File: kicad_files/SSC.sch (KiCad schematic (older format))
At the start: 9 parts, among them J1 Conn_01x09, J2 Conn_02x13_Top_Bottom, U1 74LS153, U2 74LS153

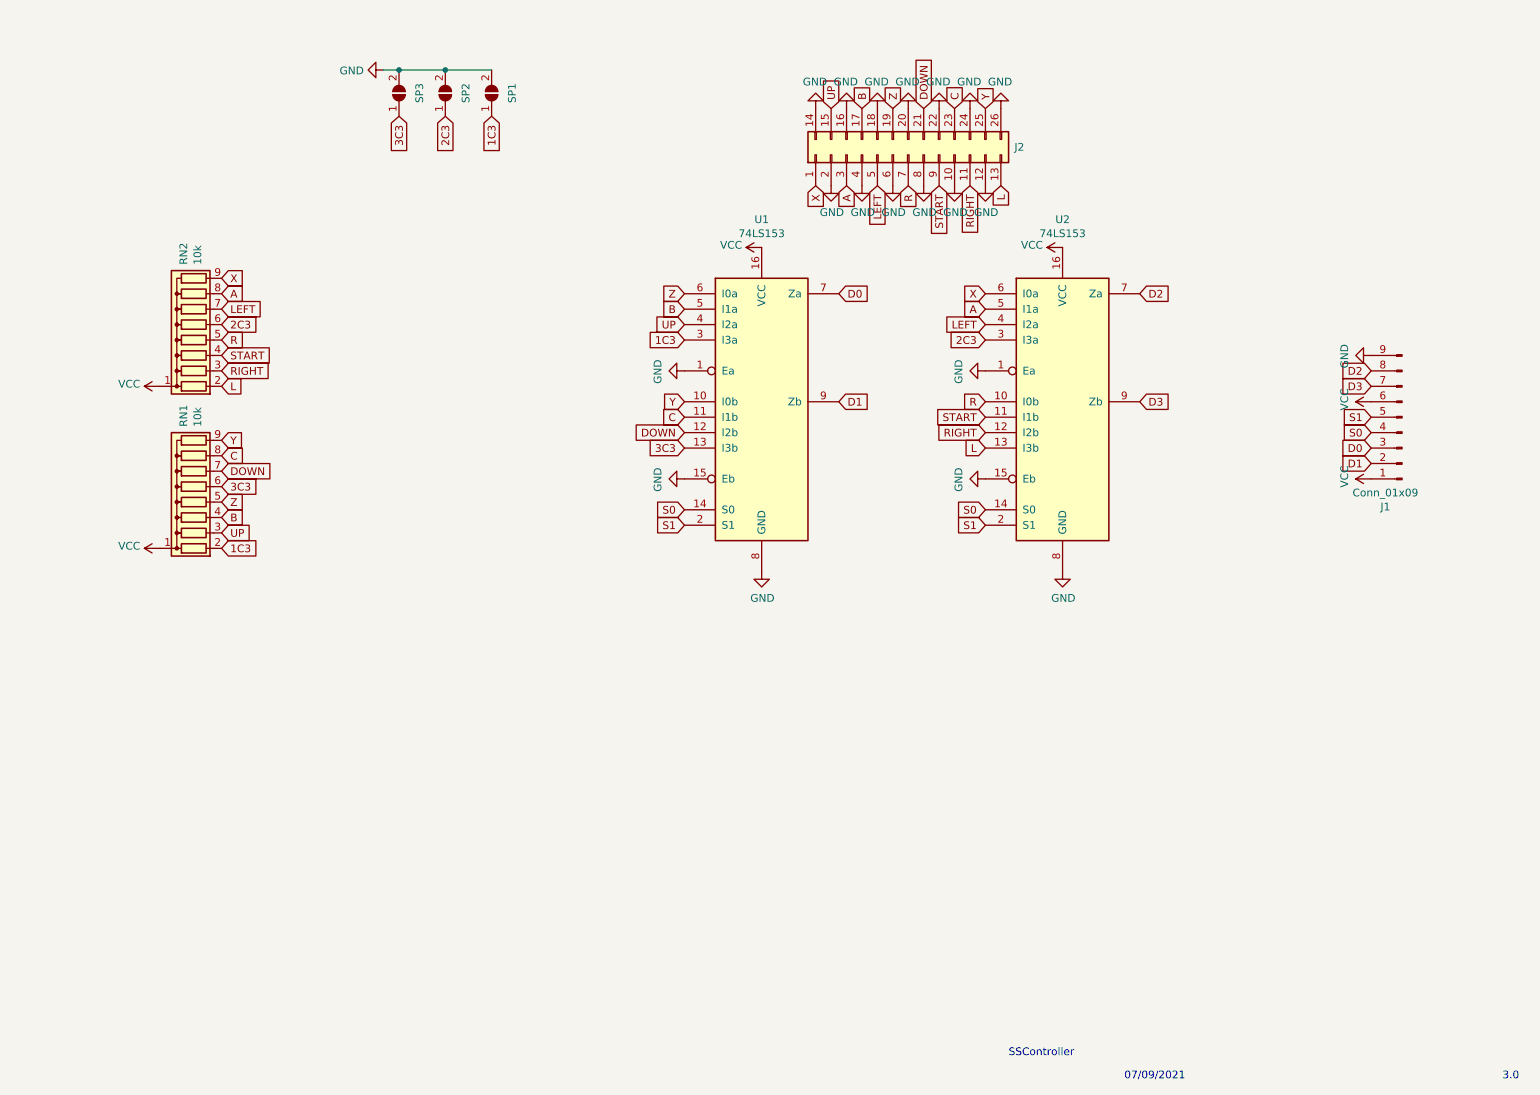
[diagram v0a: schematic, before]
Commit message: Add files via upload
Changed schematics a little and added holes to PCB.
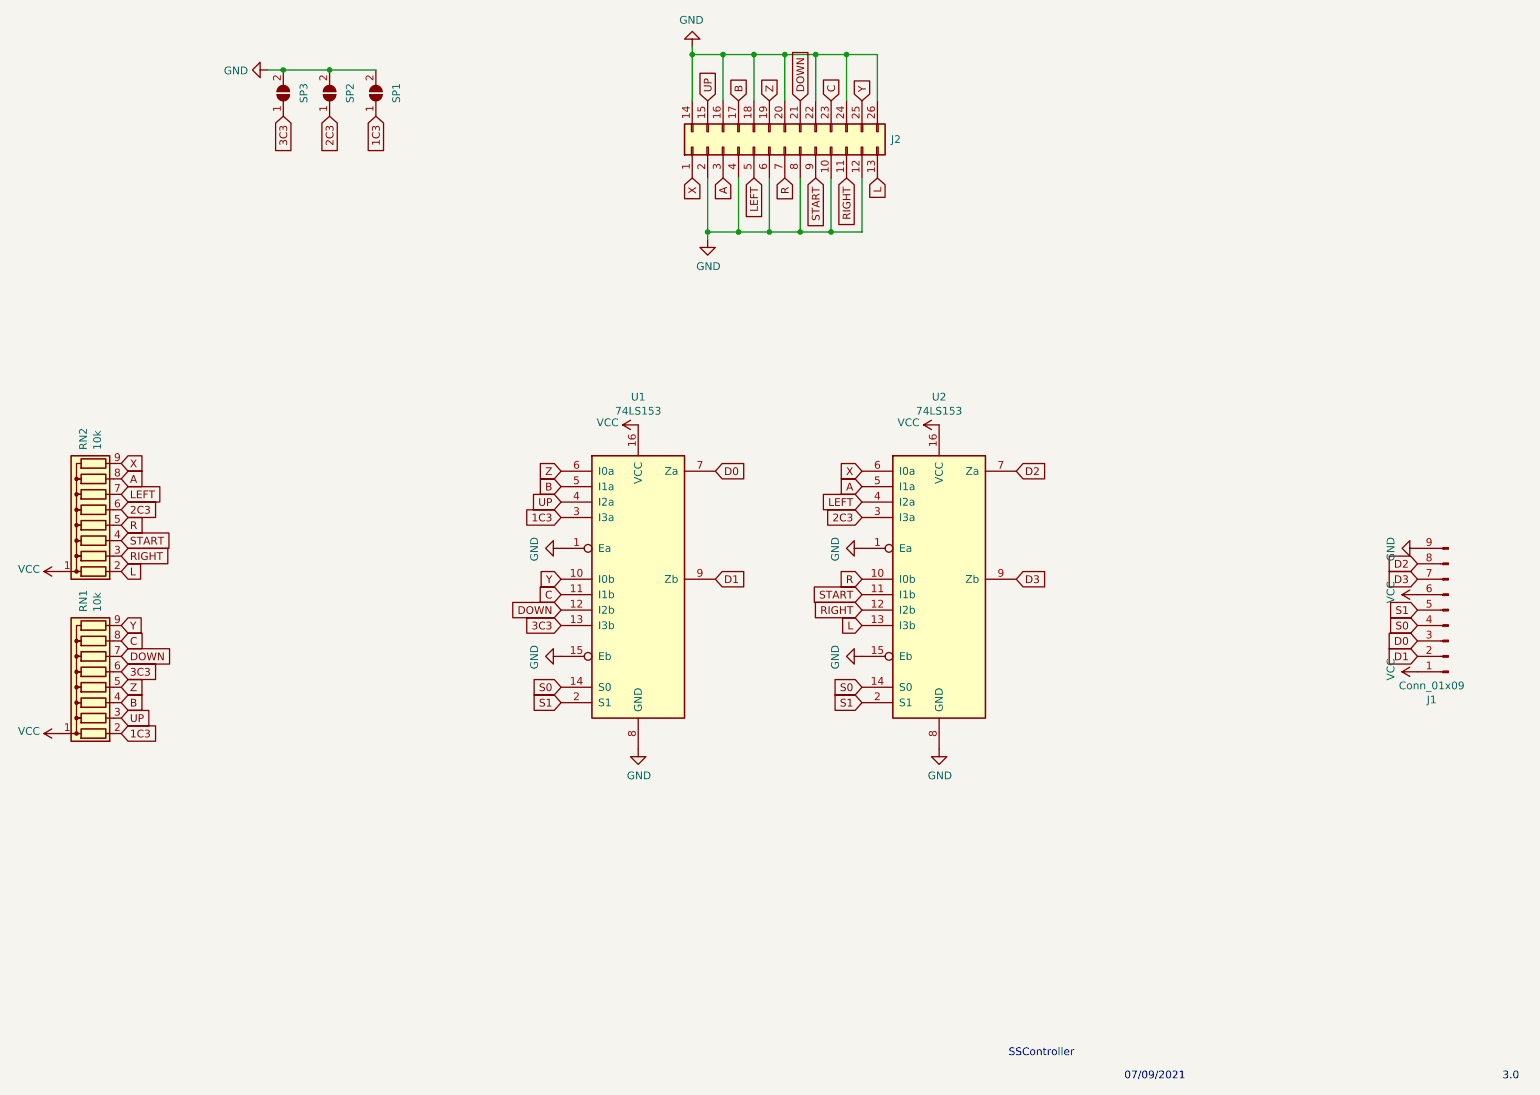
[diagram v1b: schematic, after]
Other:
- moved on the sheet: J1, J2, RN1, RN2, SP1, SP2, SP3, U1, U2
